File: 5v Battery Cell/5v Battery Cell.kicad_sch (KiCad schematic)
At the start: 38 parts, among them J1 Conn_01x02_Pin, J2 Conn_01x03_Pin, U1 TPS61023, U2 ATtiny204-SS, U3 MAX17048

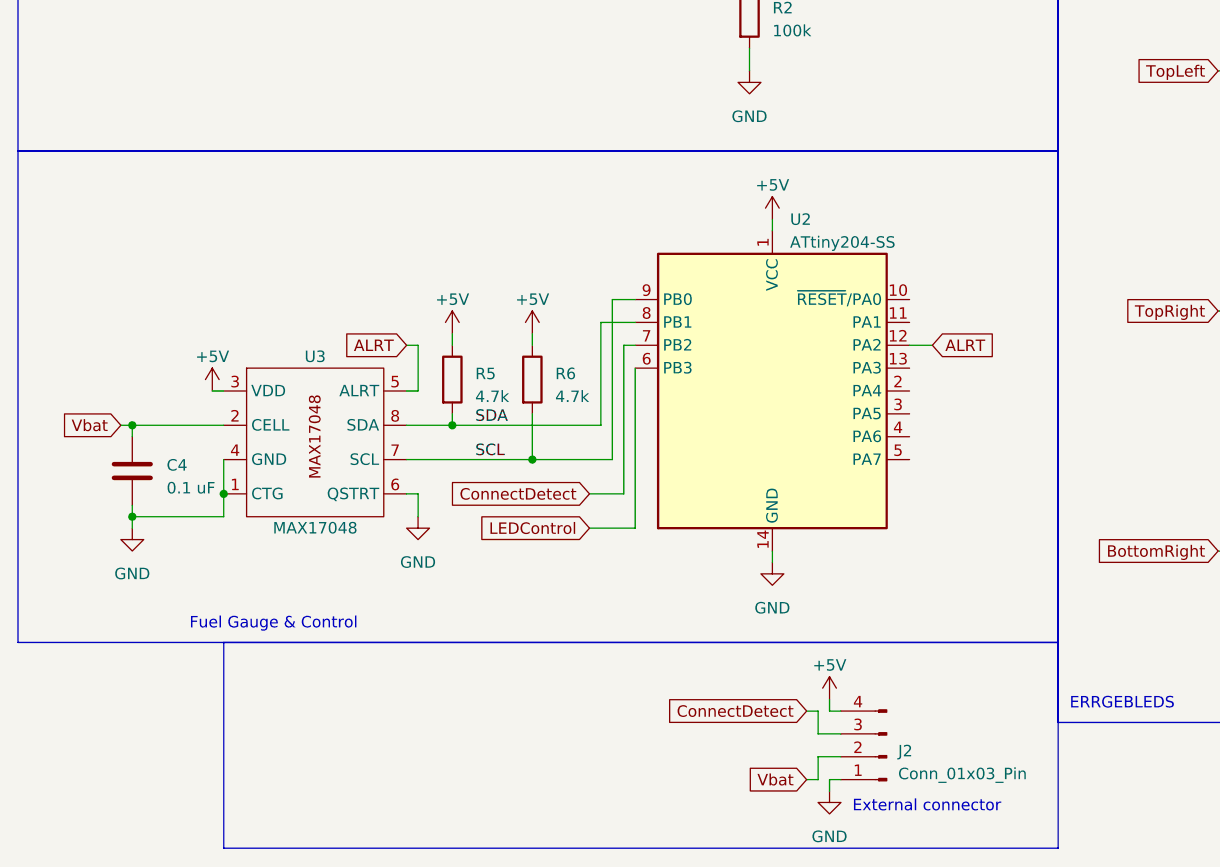
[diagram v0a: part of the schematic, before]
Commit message: Major revisions to the circuit and PCB design.
Swapped out the ATTiny204 for the AVR16DD14. Gives me extra room to work with. Updated PCB to actually be able to handle 1.5A draw from the battery, though it's never expected to reach that.
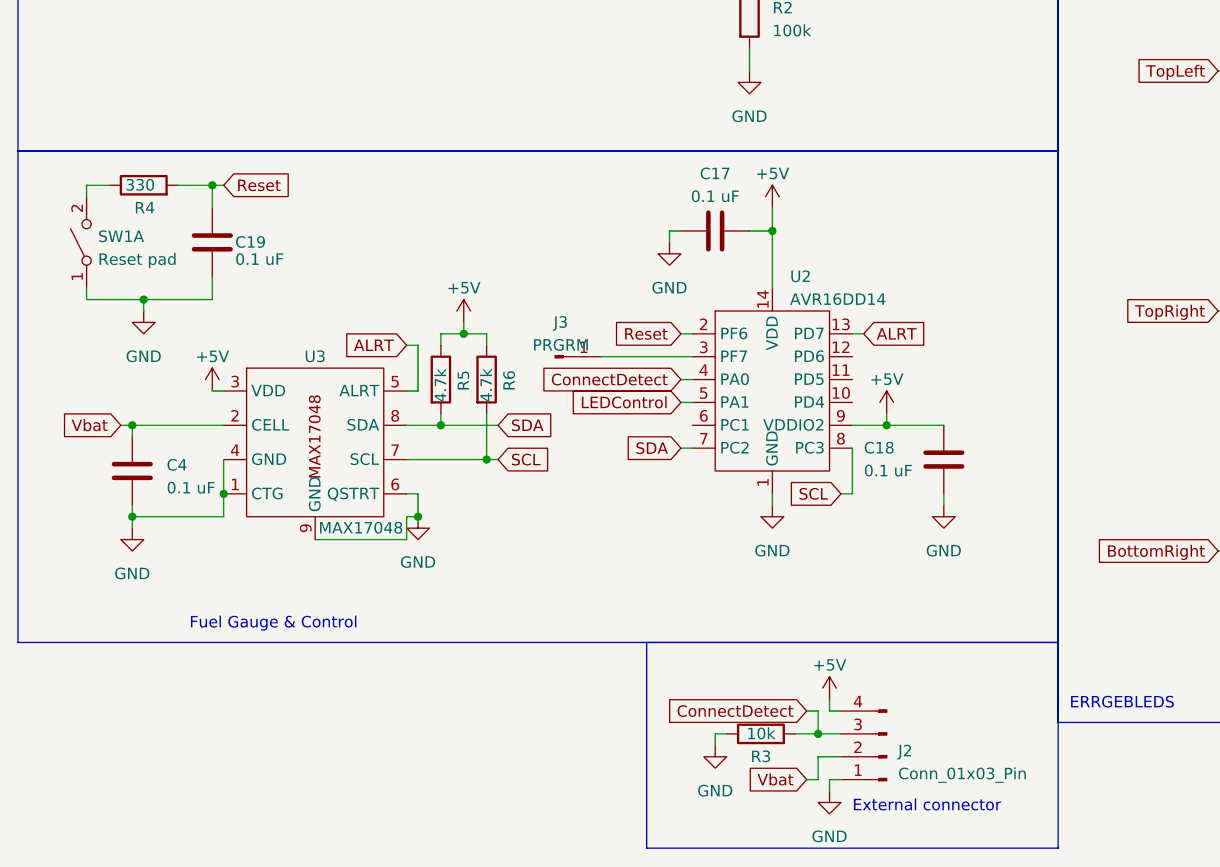
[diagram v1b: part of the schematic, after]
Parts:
- removed U2: ATtiny204-SS, Package_SO:SOIC-14_3.9x8.7mm_P1.27mm, symbol MCU_Microchip_ATtiny:ATtiny204-SS
- added C17, C18, C19: 0.1 uF, Capacitor_SMD:C_0603_1608Metric_Pad1.08x0.95mm_HandSolder, symbol Device:C
- added J3: PRGRM, Connector_Pin:Pin_D0.7mm_L6.5mm_W1.8mm_FlatFork, symbol Connector:Conn_01x01_Pin
- added R3: 10k, Resistor_SMD:R_0603_1608Metric_Pad0.98x0.95mm_HandSolder, symbol Device:R
- added R4: 330, Resistor_SMD:R_0603_1608Metric_Pad0.98x0.95mm_HandSolder, symbol Device:R
- added SW1: Reset pad, Resistor_SMD:R_0603_1608Metric_Pad0.98x0.95mm_HandSolder, symbol Switch:SW_DPST_x2
- added U2: AVR16DD14, Package_SO:SOIC-14_3.9x8.7mm_P1.27mm, symbol 000PowerCellLib:AVR16DD14
- C1, C10, C11, C12, C2, C3, C4, C5, C6, C7, C8, C9: footprint Capacitor_SMD:C_0805_2012Metric_Pad1.18x1.45mm_HandSolder -> Capacitor_SMD:C_0603_1608Metric_Pad1.08x0.95mm_HandSolder
- R1, R2, R5, R6: footprint Resistor_SMD:R_0805_2012Metric_Pad1.20x1.40mm_HandSolder -> Resistor_SMD:R_0603_1608Metric_Pad0.98x0.95mm_HandSolder
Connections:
- net +5V: now also C17.2, C18.1, U2.14 (VDD), U2.9 (VDDIO2)
- net ALRT: now also U2.13 (PD7)
- net ConnectDetect: now also R3.2, U2.4 (PA0)
- net GND: now also U3.9 (GND), C17.1, C18.2, C19.1, R3.1, SW1.1 (A), U2.1 (GND)
- net LEDControl: now also U2.5 (PA1)
- net SCL: now also U2.8 (PC3)
- net SDA: now also U2.7 (PC2)
- new net: R4.1, SW1.2 (B)
- new net: J3.1 (Pin_1), U2.3 (PF7)
- new net Reset: C19.2, R4.2, U2.2 (PF6)
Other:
- moved on the sheet: R5, R6
